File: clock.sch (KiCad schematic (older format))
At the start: 20 parts, among them SW2 SW_Push, SW3 SW_SPDT, U39 74LS04, U40 74LS08, U41 74LS32

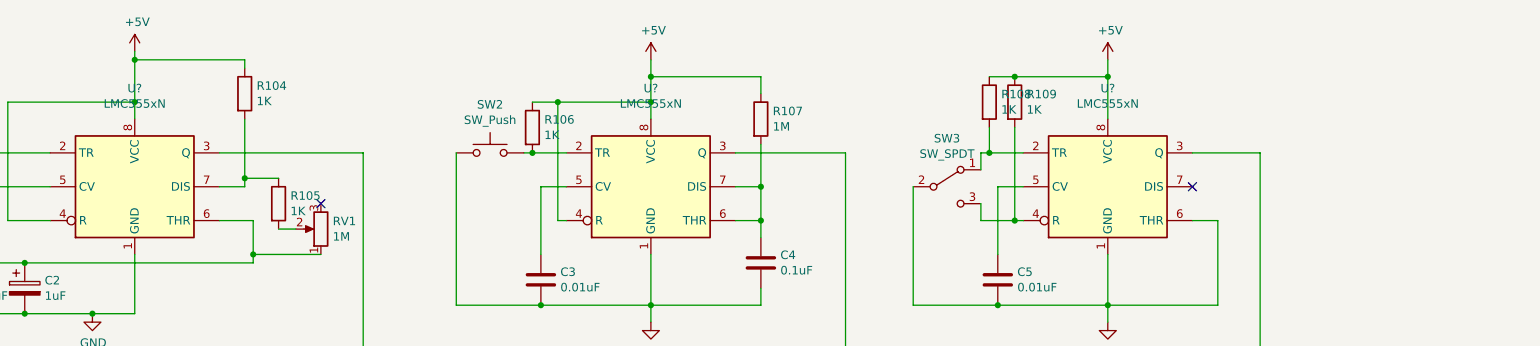
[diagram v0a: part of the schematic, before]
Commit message: added power caps
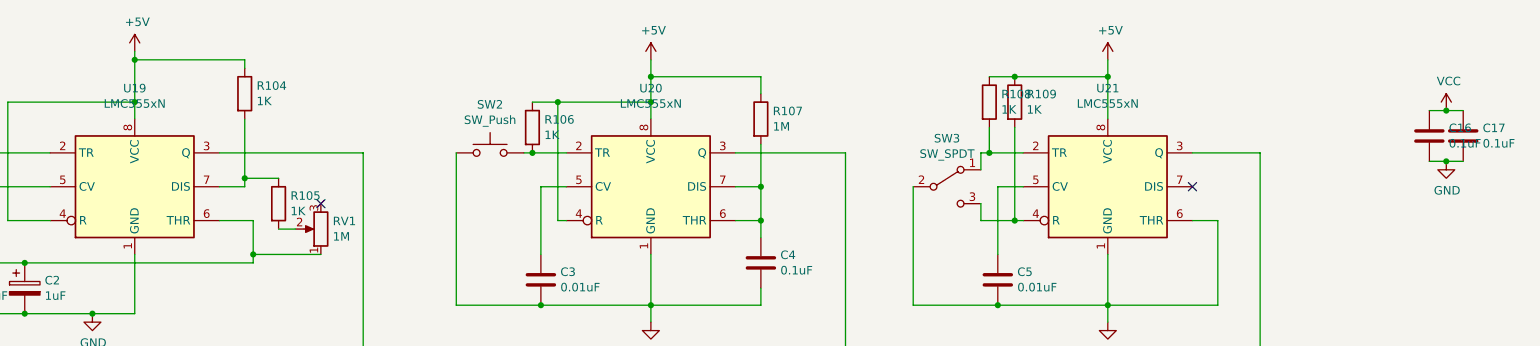
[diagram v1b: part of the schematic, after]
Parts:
- added C16, C17: 0.1uF, Capacitor_THT:CP_Axial_L10.0mm_D4.5mm_P15.00mm_Horizontal, symbol Device:C
- gave numbers to parts that had none: 3
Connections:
- net GND: now also C16.2, C17.2
- new net VCC: C16.1, C17.1
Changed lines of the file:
@@
 	1600 1900 1600 2350
 $Comp
-L Timer:LMC555xN U?
+L Timer:LMC555xN U19
 U 1 1 5F9C497D
 P 2700 1900
-F 0 "U?" H 2700 2481 50  0000 C CNN
+F 0 "U19" H 2700 2481 50  0000 C CNN
 F 1 "LMC555xN" H 2700 2390 50  0000 C CNN
 F 2 "Package_DIP:DIP-8_W7.62mm" H 3350 1500 50  0001 C CNN
@@
 $EndComp
 $Comp
-L Timer:LMC555xN U?
+L Timer:LMC555xN U20
 U 1 1 5F9DBE25
 P 5750 1900
-F 0 "U?" H 5750 2481 50  0000 C CNN
+F 0 "U20" H 5750 2481 50  0000 C CNN
 F 1 "LMC555xN" H 5750 2390 50  0000 C CNN
 F 2 "Package_DIP:DIP-8_W7.62mm" H 6400 1500 50  0001 C CNN
@@
 	2250 3550 9350 3550
 $Comp
-L Timer:LMC555xN U?
+L Timer:LMC555xN U21
 U 1 1 5F9F76EE
 P 8450 1900
-F 0 "U?" H 8450 2481 50  0000 C CNN
+F 0 "U21" H 8450 2481 50  0000 C CNN
 F 1 "LMC555xN" H 8450 2390 50  0000 C CNN
 F 2 "Package_DIP:DIP-8_W7.62mm" H 9100 1500 50  0001 C CNN
@@
 Wire Wire Line
 	6900 1700 6900 3350
+$Comp
+L 16bitCpu-rescue:VCC-power #PWR?
+U 1 1 5FAD4371
+P 10450 1450
+AR Path="/5FAD4371" Ref="#PWR?"  Part="1"
+AR Path="/5F75E433/5FAD4371" Ref="#PWR0269"  Part="1"
+F 0 "#PWR0269" H 10450 1300 50  0001 C CNN
+F 1 "VCC" H 10465 1623 50  0000 C CNN
+F 2 "" H 10450 1450 50  0001 C CNN
+F 3 "" H 10450 1450 50  0001 C CNN
+	1    10450 1450
+	1    0    0    -1
+$EndComp
+$Comp
+L 16bitCpu-rescue:GND-power #PWR?
+U 1 1 5FADA2C1
+P 10450 1750
+AR Path="/5FADA2C1" Ref="#PWR?"  Part="1"
+AR Path="/5F75E433/5FADA2C1" Ref="#PWR0270"  Part="1"
+F 0 "#PWR0270" H 10450 1500 50  0001 C CNN
+F 1 "GND" H 10455 1577 50  0000 C CNN
+F 2 "" H 10450 1750 50  0001 C CNN
+F 3 "" H 10450 1750 50  0001 C CNN
+	1    10450 1750
+	1    0    0    -1
+$EndComp
+Wire Wire Line
+	10450 1450 10550 1450
+Wire Wire Line
+	10550 1750 10450 1750
+$Comp
+L Device:C C16
+U 1 1 5FAE8A00
+P 10350 1600
+F 0 "C16" H 10465 1646 50  0000 L CNN
+F 1 "0.1uF" H 10465 1555 50  0000 L CNN
+F 2 "Capacitor_THT:CP_Axial_L10.0mm_D4.5mm_P15.00mm_Horizontal" H 10388 1450 50  0001 C CNN
+F 3 "" H 10350 1600 50  0001 C CNN
+	1    10350 1600
+	1    0    0    -1
+$EndComp
+Wire Wire Line
+	10450 1450 10350 1450
+Connection ~ 10450 1450
+Wire Wire Line
+	10350 1750 10450 1750
+Connection ~ 10450 1750
+$Comp
+L Device:C C17
+U 1 1 5FAF7273
+P 10550 1600
+F 0 "C17" H 10665 1646 50  0000 L CNN
+F 1 "0.1uF" H 10665 1555 50  0000 L CNN
+F 2 "Capacitor_THT:CP_Axial_L10.0mm_D4.5mm_P15.00mm_Horizontal" H 10588 1450 50  0001 C CNN
+F 3 "" H 10550 1600 50  0001 C CNN
+	1    10550 1600
+	1    0    0    -1
+$EndComp
 $EndSCHEMATC

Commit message: Added power connector
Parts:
- SW3: footprint ROM:DPDT-pushbutton -> ROM:SW_MINI-SPDT-SW
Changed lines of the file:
@@
 $Descr A4 11693 8268
 encoding utf-8
-Sheet 12 21
+Sheet 12 22
 Title ""
 Date ""
@@
 F 0 "SW3" H 7500 2185 50  0000 C CNN
 F 1 "SW_SPDT" H 7500 2094 50  0000 C CNN
-F 2 "ROM:DPDT-pushbutton" H 7500 1900 50  0001 C CNN
+F 2 "ROM:SW_MINI-SPDT-SW" H 7500 1900 50  0001 C CNN
 F 3 "~" H 7500 1900 50  0001 C CNN
 	1    7500 1900

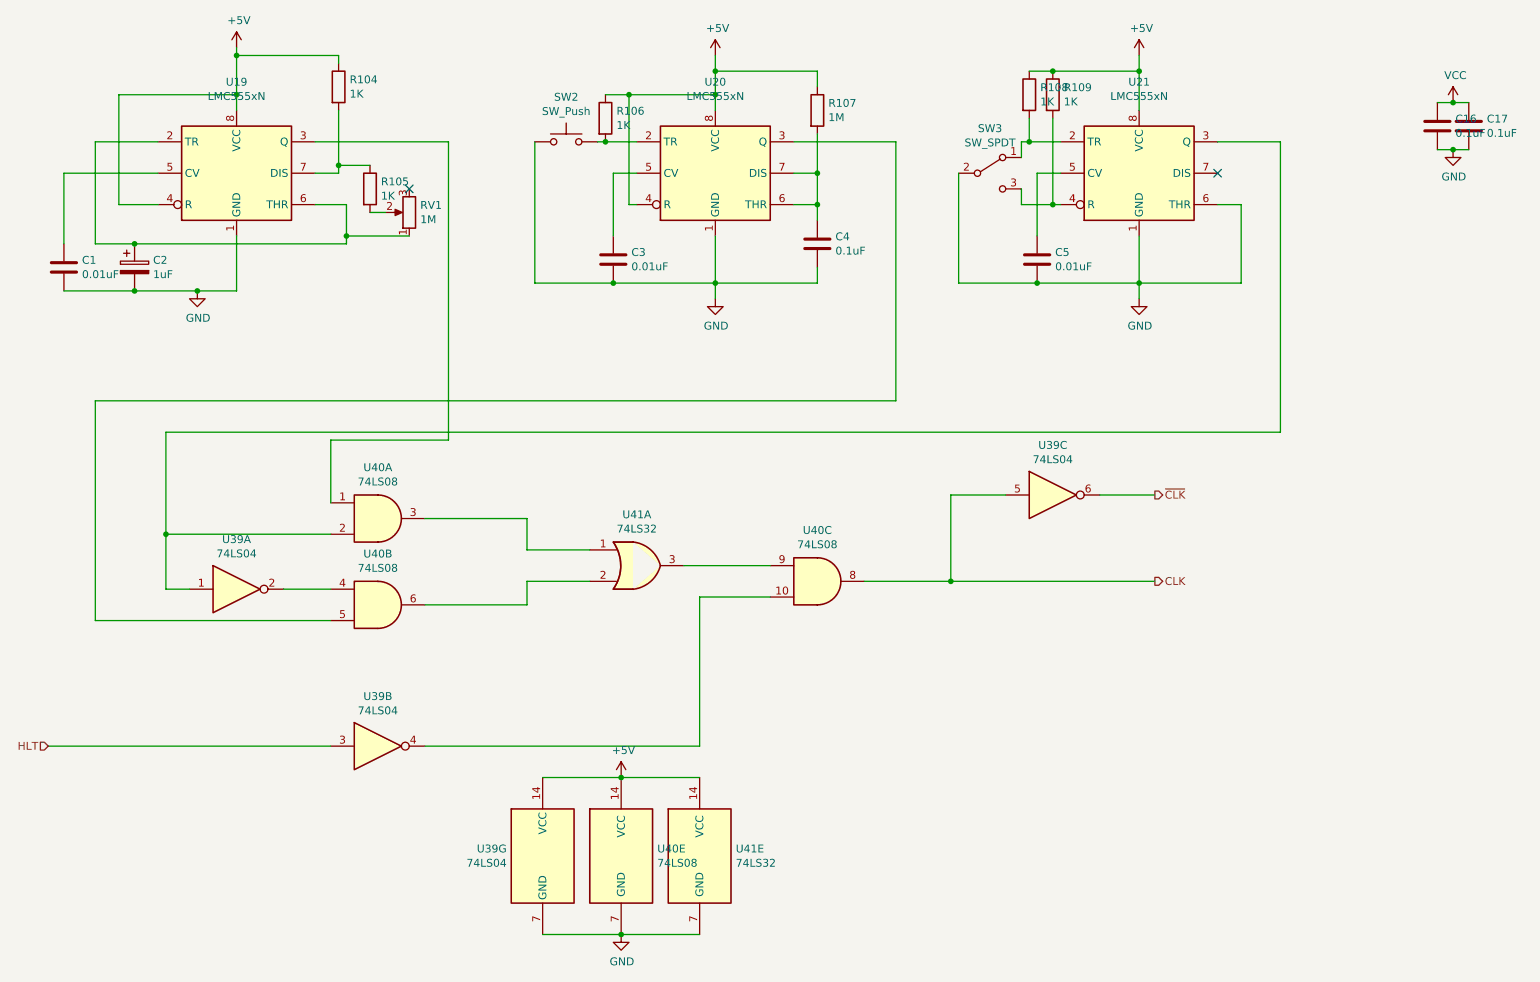
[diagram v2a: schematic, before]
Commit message: added display
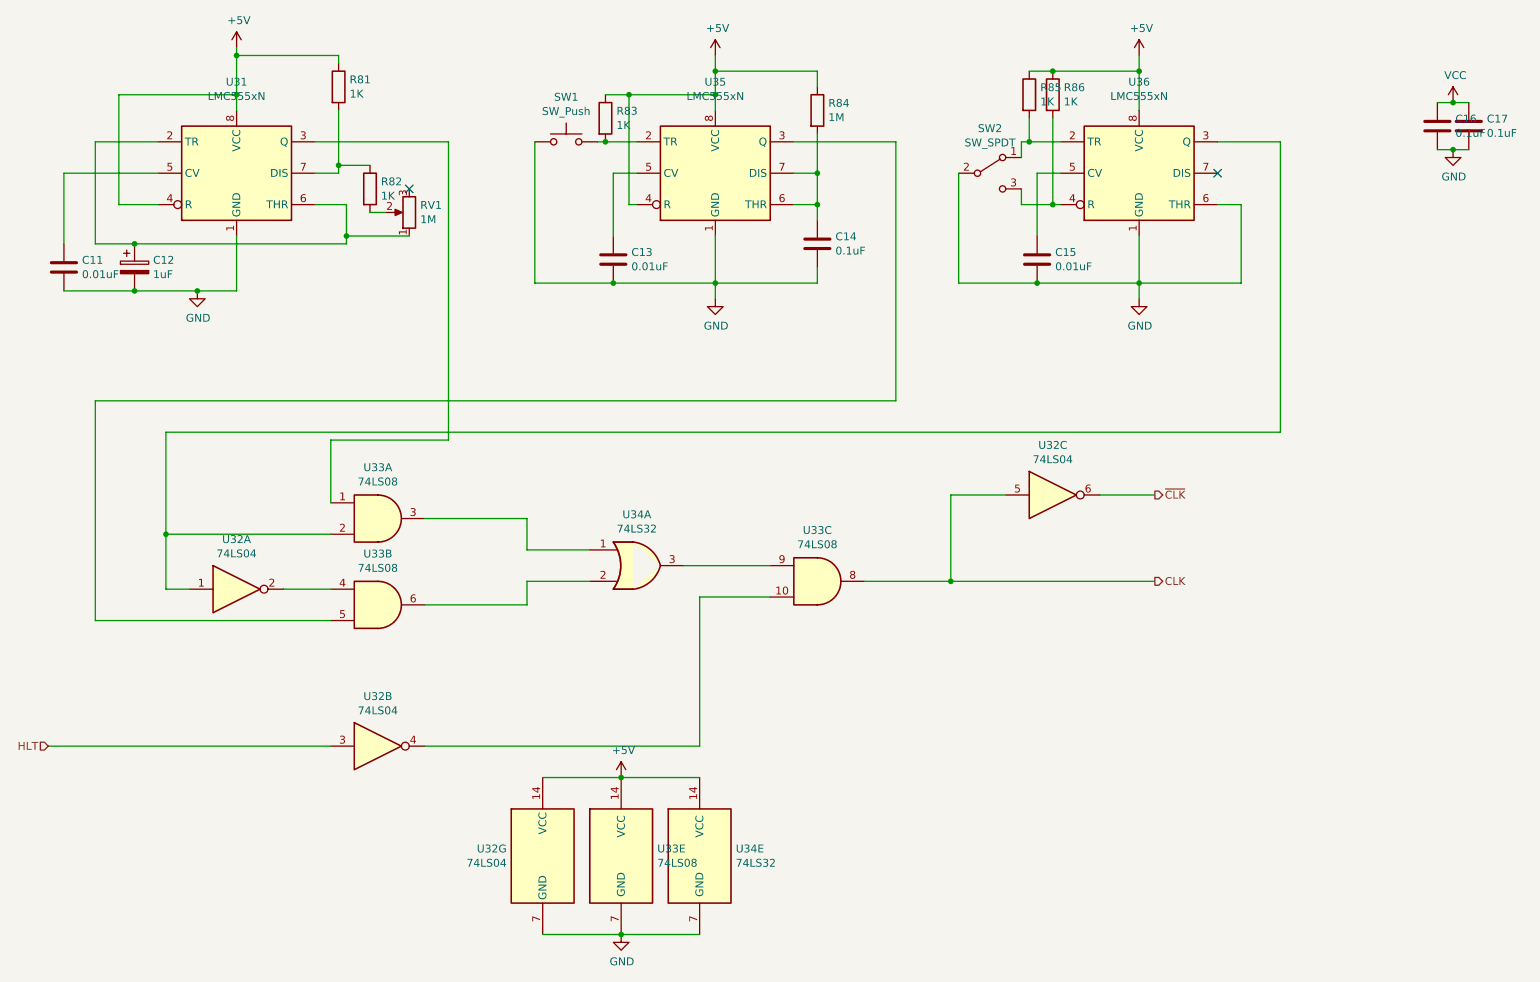
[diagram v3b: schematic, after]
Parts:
- renumbered C1 to C11, C2 to C12, C3 to C13, C4 to C14, C5 to C15, R104 to R81, R105 to R82, R106 to R83, R107 to R84, R108 to R85, R109 to R86, SW2 to SW1, SW3 to SW2, U19 to U31, U39 to U32, U40 to U33, U41 to U34, U20 to U35, U21 to U36

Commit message: added swp_x, and cleanup readme
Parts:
- removed unit 2 of U32
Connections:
- net ~HLT: now reaches U33.10
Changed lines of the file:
@@
-$Comp
-L 16bitCpu-rescue:74LS04-74xx U?
-U 2 1 5F7D01D9
-P 3600 5550
-AR Path="/5F7D01D9" Ref="U?"  Part="2"
-AR Path="/5F75E433/5F7D01D9" Ref="U32"  Part="2"
-F 0 "U32" H 3600 5867 50  0000 C CNN
-F 1 "74LS04" H 3600 5776 50  0000 C CNN
-F 2 "Package_DIP:DIP-14_W7.62mm" H 3600 5550 50  0001 C CNN
-F 3 "http://www.ti.com/lit/gpn/sn74LS08" H 3600 5550 50  0001 C CNN
-	2    3600 5550
-	1    0    0    -1
-$EndComp
 $Comp
 L 16bitCpu-rescue:74LS04-74xx U?
@@
 	5550 4400 6100 4400
 Wire Wire Line
-	3900 5550 5650 5550
-Wire Wire Line
 	5650 5550 5650 4600
 Wire Wire Line
@@
 Wire Wire Line
 	8200 3950 8550 3950
-Wire Wire Line
-	1500 5550 3300 5550
-Text HLabel 1500 5550 0    50   Input ~ 0
-HLT
+Text HLabel 2100 5550 0    50   Input ~ 0
+~HLT
 Text HLabel 8550 3950 2    50   Output ~ 0
 ~CLK
@@
 	1    0    0    -1
 $EndComp
+Wire Wire Line
+	2100 5550 5650 5550
 $EndSCHEMATC

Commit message: clean up
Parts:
- renumbered U31 to U33, U32 to U34, U33 to U35, U34 to U36, U35 to U37, U36 to U38
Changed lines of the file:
@@
 P 2700 1100
 AR Path="/5F76260D" Ref="#PWR?"  Part="1"
-AR Path="/5F75E433/5F76260D" Ref="#PWR0123"  Part="1"
-F 0 "#PWR0123" H 2700 950 50  0001 C CNN
+AR Path="/5F75E433/5F76260D" Ref="#PWR0131"  Part="1"
+F 0 "#PWR0131" H 2700 950 50  0001 C CNN
 F 1 "+5V" H 2715 1273 50  0000 C CNN
 F 2 "" H 2700 1100 50  0001 C CNN
@@
 P 5750 2700
 AR Path="/5F763381" Ref="#PWR?"  Part="1"
-AR Path="/5F75E433/5F763381" Ref="#PWR0127"  Part="1"
-F 0 "#PWR0127" H 5750 2450 50  0001 C CNN
+AR Path="/5F75E433/5F763381" Ref="#PWR0135"  Part="1"
+F 0 "#PWR0135" H 5750 2450 50  0001 C CNN
 F 1 "GND" H 5755 2527 50  0000 C CNN
 F 2 "" H 5750 2700 50  0001 C CNN
@@
 P 2450 2650
 AR Path="/5F7634B3" Ref="#PWR?"  Part="1"
-AR Path="/5F75E433/5F7634B3" Ref="#PWR0122"  Part="1"
-F 0 "#PWR0122" H 2450 2400 50  0001 C CNN
+AR Path="/5F75E433/5F7634B3" Ref="#PWR0130"  Part="1"
+F 0 "#PWR0130" H 2450 2400 50  0001 C CNN
 F 1 "GND" H 2455 2477 50  0000 C CNN
 F 2 "" H 2450 2650 50  0001 C CNN
@@
 P 5750 1150
 AR Path="/5F76F8D8" Ref="#PWR?"  Part="1"
-AR Path="/5F75E433/5F76F8D8" Ref="#PWR0126"  Part="1"
-F 0 "#PWR0126" H 5750 1000 50  0001 C CNN
+AR Path="/5F75E433/5F76F8D8" Ref="#PWR0134"  Part="1"
+F 0 "#PWR0134" H 5750 1000 50  0001 C CNN
 F 1 "+5V" H 5765 1323 50  0000 C CNN
 F 2 "" H 5750 1150 50  0001 C CNN
@@
 P 8450 2700
 AR Path="/5F785279" Ref="#PWR?"  Part="1"
-AR Path="/5F75E433/5F785279" Ref="#PWR0129"  Part="1"
-F 0 "#PWR0129" H 8450 2450 50  0001 C CNN
+AR Path="/5F75E433/5F785279" Ref="#PWR0137"  Part="1"
+F 0 "#PWR0137" H 8450 2450 50  0001 C CNN
 F 1 "GND" H 8455 2527 50  0000 C CNN
 F 2 "" H 8450 2700 50  0001 C CNN
@@
 P 8450 1150
 AR Path="/5F78527F" Ref="#PWR?"  Part="1"
-AR Path="/5F75E433/5F78527F" Ref="#PWR0128"  Part="1"
-F 0 "#PWR0128" H 8450 1000 50  0001 C CNN
+AR Path="/5F75E433/5F78527F" Ref="#PWR0136"  Part="1"
+F 0 "#PWR0136" H 8450 1000 50  0001 C CNN
 F 1 "+5V" H 8465 1323 50  0000 C CNN
 F 2 "" H 8450 1150 50  0001 C CNN
@@
 P 3600 4100
 AR Path="/5F7BE3EA" Ref="U?"  Part="1"
-AR Path="/5F75E433/5F7BE3EA" Ref="U33"  Part="1"
-F 0 "U33" H 3600 4425 50  0000 C CNN
+AR Path="/5F75E433/5F7BE3EA" Ref="U35"  Part="1"
+F 0 "U35" H 3600 4425 50  0000 C CNN
 F 1 "74LS08" H 3600 4334 50  0000 C CNN
 F 2 "Package_DIP:DIP-14_W7.62mm" H 3600 4100 50  0001 C CNN
@@
 P 3600 4650
 AR Path="/5F7C112B" Ref="U?"  Part="2"
-AR Path="/5F75E433/5F7C112B" Ref="U33"  Part="2"
-F 0 "U33" H 3600 4975 50  0000 C CNN
+AR Path="/5F75E433/5F7C112B" Ref="U35"  Part="2"
+F 0 "U35" H 3600 4975 50  0000 C CNN
 F 1 "74LS08" H 3600 4884 50  0000 C CNN
 F 2 "Package_DIP:DIP-14_W7.62mm" H 3600 4650 50  0001 C CNN
@@
 P 6400 4500
 AR Path="/5F7C255C" Ref="U?"  Part="3"
-AR Path="/5F75E433/5F7C255C" Ref="U33"  Part="3"
-F 0 "U33" H 6400 4825 50  0000 C CNN
+AR Path="/5F75E433/5F7C255C" Ref="U35"  Part="3"
+F 0 "U35" H 6400 4825 50  0000 C CNN
 F 1 "74LS08" H 6400 4734 50  0000 C CNN
 F 2 "Package_DIP:DIP-14_W7.62mm" H 6400 4500 50  0001 C CNN
@@
 P 5250 4400
 AR Path="/5F7C6F12" Ref="U?"  Part="1"
-AR Path="/5F75E433/5F7C6F12" Ref="U34"  Part="1"
-F 0 "U34" H 5250 4725 50  0000 C CNN
+AR Path="/5F75E433/5F7C6F12" Ref="U36"  Part="1"
+F 0 "U36" H 5250 4725 50  0000 C CNN
 F 1 "74LS32" H 5250 4634 50  0000 C CNN
 F 2 "Package_DIP:DIP-14_W7.62mm" H 5250 4400 50  0001 C CNN
@@
 P 2700 4550
 AR Path="/5F7CE7FD" Ref="U?"  Part="1"
-AR Path="/5F75E433/5F7CE7FD" Ref="U32"  Part="1"
-F 0 "U32" H 2700 4867 50  0000 C CNN
+AR Path="/5F75E433/5F7CE7FD" Ref="U34"  Part="1"
+F 0 "U34" H 2700 4867 50  0000 C CNN
 F 1 "74LS04" H 2700 4776 50  0000 C CNN
 F 2 "Package_DIP:DIP-14_W7.62mm" H 2700 4550 50  0001 C CNN
@@
 P 7900 3950
 AR Path="/5F7D1AFC" Ref="U?"  Part="3"
-AR Path="/5F75E433/5F7D1AFC" Ref="U32"  Part="3"
-F 0 "U32" H 7900 4267 50  0000 C CNN
+AR Path="/5F75E433/5F7D1AFC" Ref="U34"  Part="3"
+F 0 "U34" H 7900 4267 50  0000 C CNN
 F 1 "74LS04" H 7900 4176 50  0000 C CNN
 F 2 "Package_DIP:DIP-14_W7.62mm" H 7900 3950 50  0001 C CNN
@@
 P 5150 5750
 AR Path="/6081D7D4" Ref="#PWR?"  Part="1"
-AR Path="/5F75E433/6081D7D4" Ref="#PWR0124"  Part="1"
-F 0 "#PWR0124" H 5150 5600 50  0001 C CNN
+AR Path="/5F75E433/6081D7D4" Ref="#PWR0132"  Part="1"
+F 0 "#PWR0132" H 5150 5600 50  0001 C CNN
 F 1 "+5V" H 5165 5923 50  0000 C CNN
 F 2 "" H 5150 5750 50  0001 C CNN
@@
 P 5150 6750
 AR Path="/6081E349" Ref="#PWR?"  Part="1"
-AR Path="/5F75E433/6081E349" Ref="#PWR0125"  Part="1"
-F 0 "#PWR0125" H 5150 6500 50  0001 C CNN
+AR Path="/5F75E433/6081E349" Ref="#PWR0133"  Part="1"
+F 0 "#PWR0133" H 5150 6500 50  0001 C CNN
 F 1 "GND" H 5155 6577 50  0000 C CNN
 F 2 "" H 5150 6750 50  0001 C CNN
@@
 P 4650 6250
 AR Path="/6085491F" Ref="U?"  Part="7"
-AR Path="/5F75E433/6085491F" Ref="U32"  Part="7"
-F 0 "U32" H 4421 6296 50  0000 R CNN
+AR Path="/5F75E433/6085491F" Ref="U34"  Part="7"
+F 0 "U34" H 4421 6296 50  0000 R CNN
 F 1 "74LS04" H 4421 6205 50  0000 R CNN
 F 2 "Package_DIP:DIP-14_W7.62mm" H 4650 6250 50  0001 C CNN
@@
 P 5150 6250
 AR Path="/6085870D" Ref="U?"  Part="5"
-AR Path="/5F75E433/6085870D" Ref="U33"  Part="5"
-F 0 "U33" H 5380 6296 50  0000 L CNN
+AR Path="/5F75E433/6085870D" Ref="U35"  Part="5"
+F 0 "U35" H 5380 6296 50  0000 L CNN
 F 1 "74LS08" H 5380 6205 50  0000 L CNN
 F 2 "Package_DIP:DIP-14_W7.62mm" H 5150 6250 50  0001 C CNN
@@
 P 5650 6250
 AR Path="/608654F6" Ref="U?"  Part="5"
-AR Path="/5F75E433/608654F6" Ref="U34"  Part="5"
-F 0 "U34" H 5880 6296 50  0000 L CNN
+AR Path="/5F75E433/608654F6" Ref="U36"  Part="5"
+F 0 "U36" H 5880 6296 50  0000 L CNN
 F 1 "74LS32" H 5880 6205 50  0000 L CNN
 F 2 "Package_DIP:DIP-14_W7.62mm" H 5650 6250 50  0001 C CNN
@@
 	1600 1900 1600 2350
 $Comp
-L Timer:LMC555xN U31
+L Timer:LMC555xN U33
 U 1 1 5F9C497D
 P 2700 1900
-F 0 "U31" H 2700 2481 50  0000 C CNN
+F 0 "U33" H 2700 2481 50  0000 C CNN
 F 1 "LMC555xN" H 2700 2390 50  0000 C CNN
 F 2 "Package_DIP:DIP-8_W7.62mm" H 3350 1500 50  0001 C CNN
@@
 $EndComp
 $Comp
-L Timer:LMC555xN U35
+L Timer:LMC555xN U37
 U 1 1 5F9DBE25
 P 5750 1900
-F 0 "U35" H 5750 2481 50  0000 C CNN
+F 0 "U37" H 5750 2481 50  0000 C CNN
 F 1 "LMC555xN" H 5750 2390 50  0000 C CNN
 F 2 "Package_DIP:DIP-8_W7.62mm" H 6400 1500 50  0001 C CNN
@@
 	2250 3550 9350 3550
 $Comp
-L Timer:LMC555xN U36
+L Timer:LMC555xN U38
 U 1 1 5F9F76EE
 P 8450 1900
-F 0 "U36" H 8450 2481 50  0000 C CNN
+F 0 "U38" H 8450 2481 50  0000 C CNN
 F 1 "LMC555xN" H 8450 2390 50  0000 C CNN
 F 2 "Package_DIP:DIP-8_W7.62mm" H 9100 1500 50  0001 C CNN
@@
 P 10450 1450
 AR Path="/5FAD4371" Ref="#PWR?"  Part="1"
-AR Path="/5F75E433/5FAD4371" Ref="#PWR0130"  Part="1"
-F 0 "#PWR0130" H 10450 1300 50  0001 C CNN
+AR Path="/5F75E433/5FAD4371" Ref="#PWR0138"  Part="1"
+F 0 "#PWR0138" H 10450 1300 50  0001 C CNN
 F 1 "VCC" H 10465 1623 50  0000 C CNN
 F 2 "" H 10450 1450 50  0001 C CNN
@@
 P 10450 1750
 AR Path="/5FADA2C1" Ref="#PWR?"  Part="1"
-AR Path="/5F75E433/5FADA2C1" Ref="#PWR0131"  Part="1"
-F 0 "#PWR0131" H 10450 1500 50  0001 C CNN
+AR Path="/5F75E433/5FADA2C1" Ref="#PWR0139"  Part="1"
+F 0 "#PWR0139" H 10450 1500 50  0001 C CNN
 F 1 "GND" H 10455 1577 50  0000 C CNN
 F 2 "" H 10450 1750 50  0001 C CNN
